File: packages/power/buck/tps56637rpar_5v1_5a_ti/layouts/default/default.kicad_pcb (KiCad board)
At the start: 2 copper layers, 10 parts

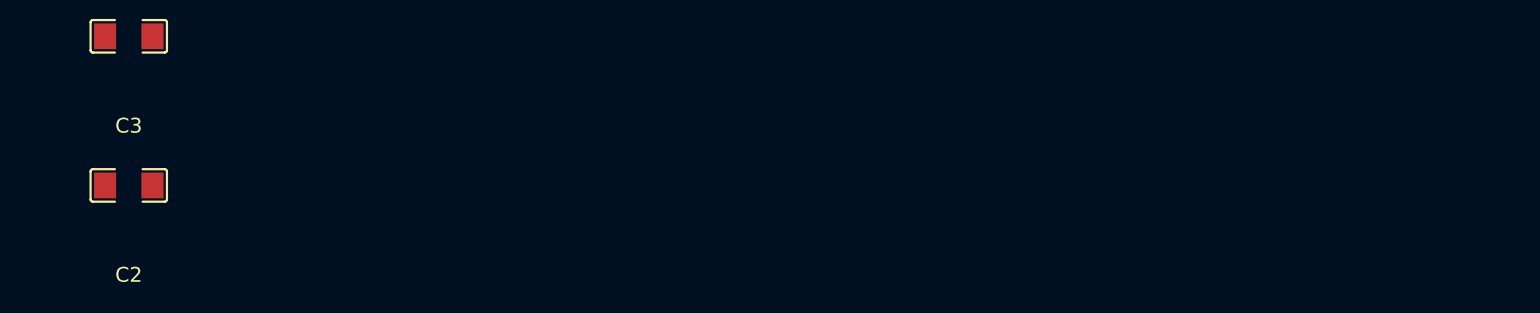
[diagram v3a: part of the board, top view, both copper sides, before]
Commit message: Keep package outputs aligned with production BOMs and documented parts
This removes top-level package example targets and their checked-in example
layouts so the library tracks the maintained default package outputs only.
It also adds minimal KiCad project files for each default layout and a
root components inventory derived from the top-level default BOMs, then
links that inventory from the repository guidance and README so future
part changes have one canonical summary.

Constraint: Package inventories must reflect explicit LCSC-traceable default BOM selections
Constraint: Default layouts need a KiCad project file in each package layout directory
Rejected: Keep example builds and layouts alongside default outputs | duplicated maintenance burden with little library value
Rejected: Build the component inventory from vendored part folders | would include non-fitted or non-purchasable items instead of actual package BOM contents
Confidence: high
Scope-risk: moderate
Reversibility: clean
Directive: When top-level package BOM contents change, update components_list.md in the same change
Tested:  in all 13 top-level packages
Tested:  for each added
Tested: Python validation that components_list.md LCSC codes exactly match all top-level default BOM JSON files
Not-tested: Interactive KiCad GUI opening of every project file
Not-tested: Any regenerated example targets or example layout workflows
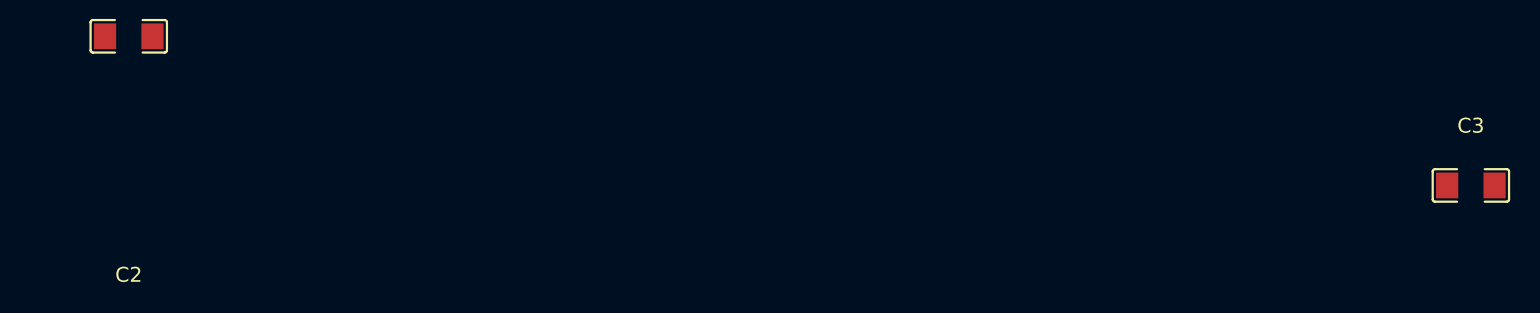
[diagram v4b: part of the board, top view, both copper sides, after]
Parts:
- moved C3 90.0 mm to (100.0, -50.0)
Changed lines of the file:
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@@
 	(footprint "Murata_Electronics_GRM31CR61H106KA12L:C1206"
 		(layer "F.Cu")
-		(at 10 -50 0)
+		(at 100 -50 0)
 		(property "Reference" "C3"
 			(at 0 -4)

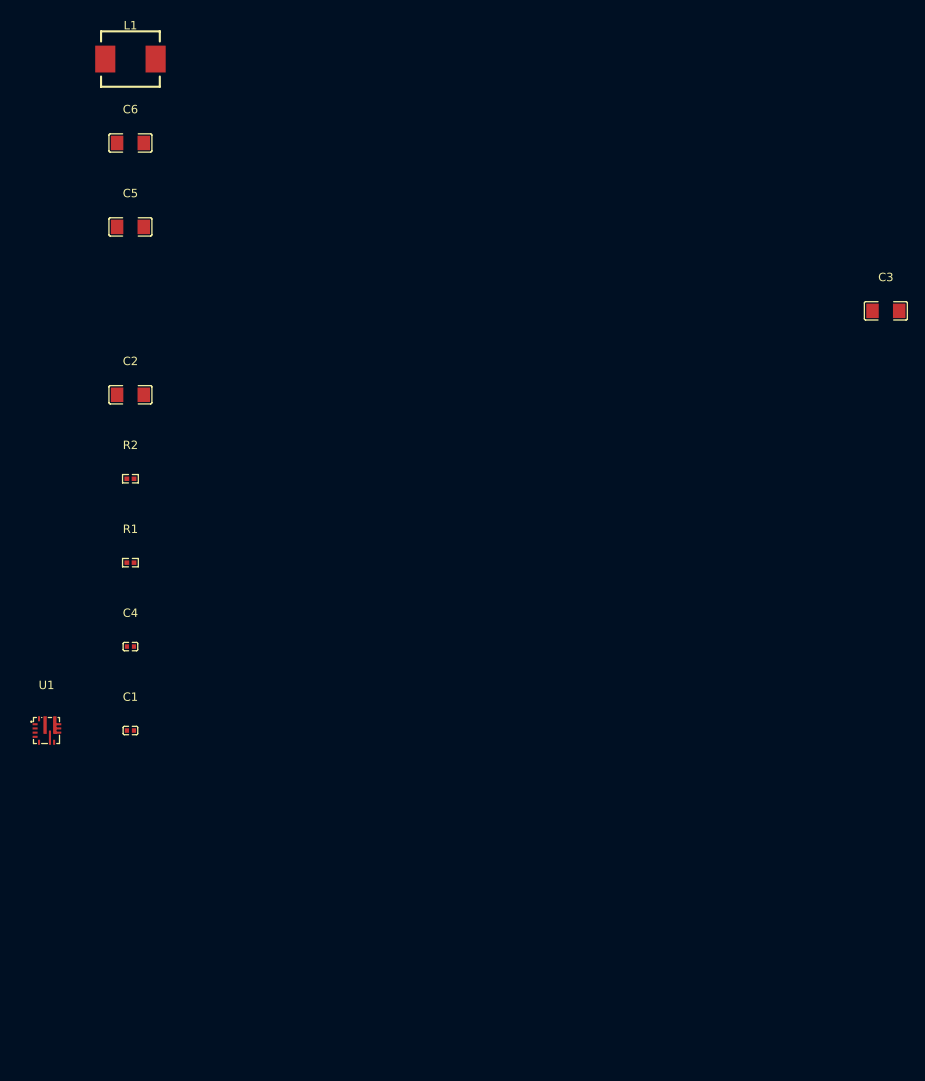
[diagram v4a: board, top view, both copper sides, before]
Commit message: 22uF cap update, TPS56637 update
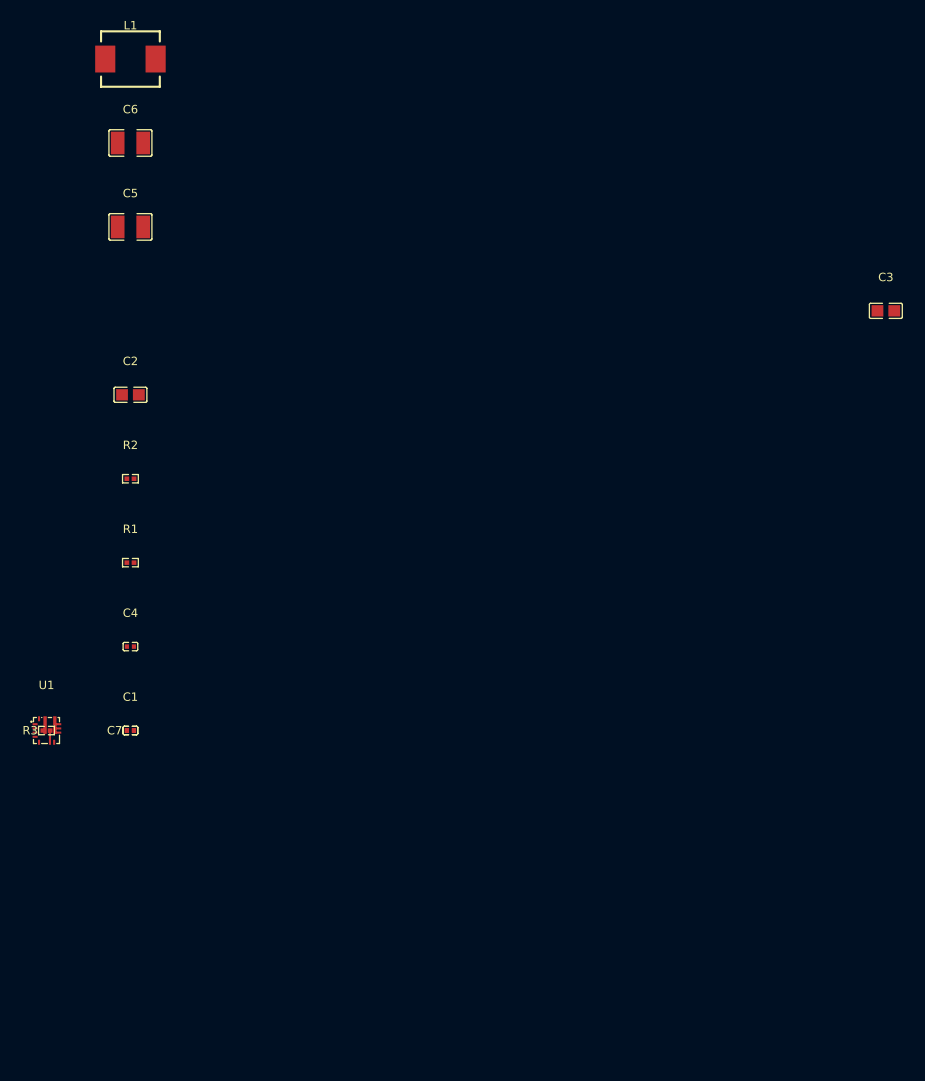
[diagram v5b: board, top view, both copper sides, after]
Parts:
- added C7: , Murata_Electronics_GRM1555C1H101JA01D:C0402, F.Cu at (10.0, 0.00)
- added R3: , YAGEO_RC0402FR_0720KL:R0402, F.Cu at (0.00, 0.00)
- C2, C3: footprint Murata_Electronics_GRM31CR61H106KA12L:C1206 -> Murata_Electronics_GRM21BR61H106KE43L:C0805
- C5, C6: footprint Murata_Electronics_GRM31CR61E226KE15L:C1206 -> Murata_Electronics_GRM32ER71E226KE15L:C1210

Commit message: TPS56637 layout
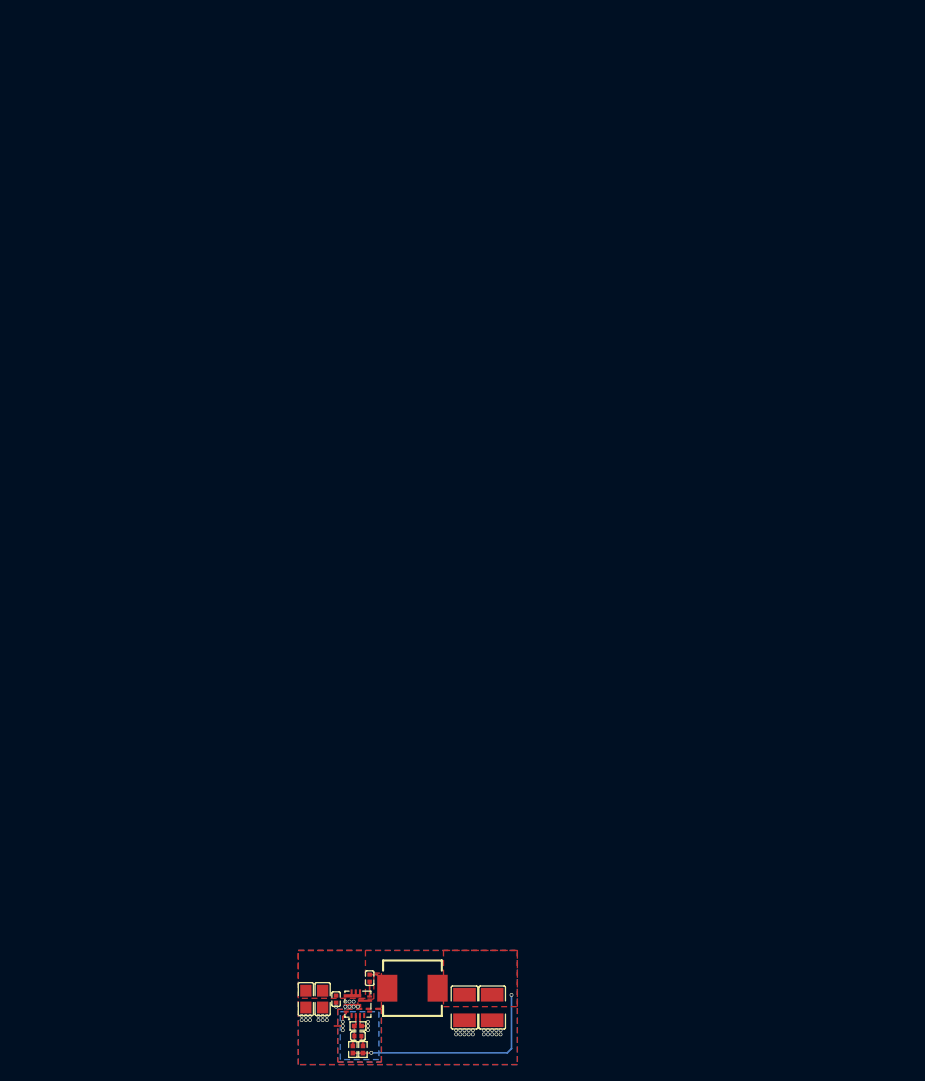
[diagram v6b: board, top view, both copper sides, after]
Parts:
- moved L1 115.7 mm to (43.6, 30.7)
- moved C6 110.4 mm to (49.8, 33.0), turned to -90 degrees
- moved C3 107.2 mm to (30.9, 32.0), turned to -90 degrees
- moved C5 102.5 mm to (53.1, 33.0), turned to -90 degrees
- moved C2 75.6 mm to (32.9, 32.0), turned to -90 degrees
- moved R2 73.0 mm to (36.5, 38.0), turned to 90 degrees
- moved R1 61.5 mm to (37.1, 35.2)
- moved R3 53.5 mm to (37.7, 38.0), turned to 90 degrees
- moved U1 49.4 mm to (37.1, 32.6), turned to 90 degrees
- moved C4 48.6 mm to (34.5, 32.0), turned to -90 degrees
- moved C7 45.4 mm to (37.1, 36.4), turned to 180 degrees
- moved C1 41.0 mm to (38.5, 29.5), turned to 90 degrees
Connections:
- U1 pad 10: MODE -> lv
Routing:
- net power_out-hv: track 0.00 -> 25.5 mm, vias 0 -> 2
- net lv: track 0.00 -> 6.46 mm, vias 0 -> 46
- net 2: track 0.00 -> 3.86 mm
- net SW: track 0.00 -> 3.01 mm
- net BOOT: track 0.00 -> 1.77 mm
- net 1: track 0.00 -> 1.34 mm
- added copper zone on F.Cu, net SW
- added copper zone on F.Cu, net hv
- added copper zone on B.Cu, net lv
- added copper zone on F.Cu, net lv
- added copper zone on In1.Cu, net lv
- added copper zone on In2.Cu, net lv
- added copper zone on F.Cu, net power_out-hv
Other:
- copper layers 2 -> 4

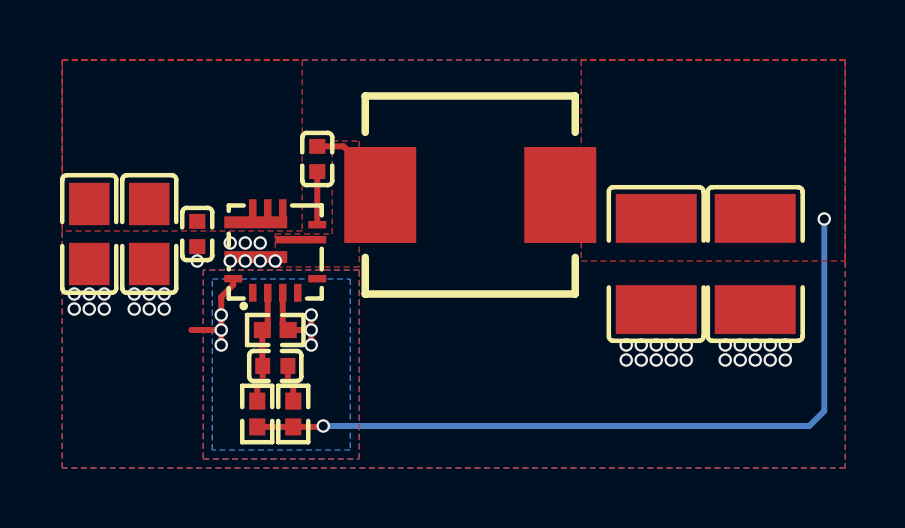
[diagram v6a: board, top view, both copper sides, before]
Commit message: TPS56637 update
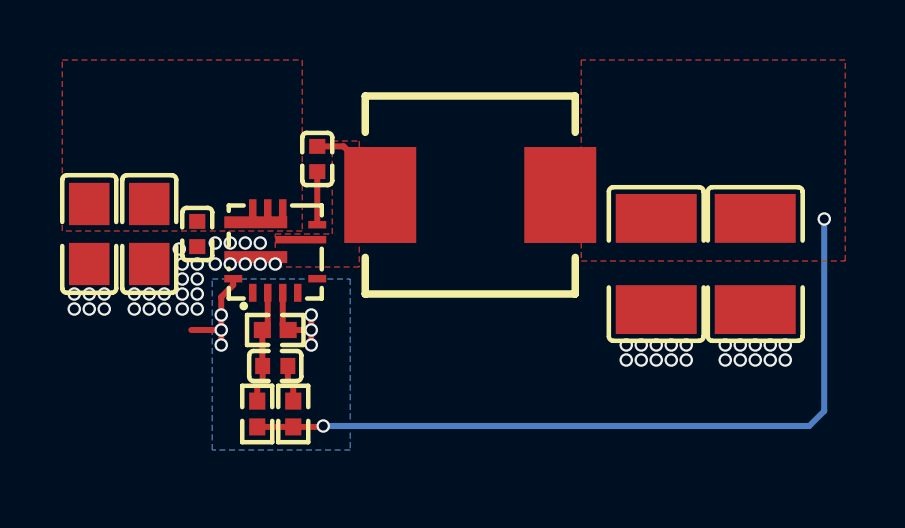
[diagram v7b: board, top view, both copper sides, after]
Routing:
- net lv: vias 46 -> 56
- removed copper zone on F.Cu, net lv
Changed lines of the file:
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@@
+	)
+	(via
+		(at 34 33.5)
+		(size 0.45)
+		(drill 0.3)
+		(layers "F.Cu" "B.Cu")
+		(free yes)
+		(net 6)
 	)
 	(via
@@
 	)
 	(via
+		(at 35.1 33)
+		(size 0.45)
+		(drill 0.3)
+		(layers "F.Cu" "B.Cu")
+		(free yes)
+		(net 6)
+	)
+	(via
 		(at 31.4 34.5)
 		(size 0.45)
@@
 	)
 	(via
+		(at 33.9 32.5)
+		(size 0.45)
+		(drill 0.3)
+		(layers "F.Cu" "B.Cu")
+		(free yes)
+		(net 6)
+	)
+	(via
 		(at 50.8 35.7)
 		(size 0.45)
@@
 	)
 	(via
-		(at 35.6 32.9)
+		(at 35.6 33)
 		(size 0.45)
 		(drill 0.3)
@@
 	)
 	(via
-		(at 37.1 32.9)
+		(at 37.1 33)
 		(size 0.45)
 		(drill 0.3)
@@
 	)
 	(via
+		(at 34 34.5)
+		(size 0.45)
+		(drill 0.3)
+		(layers "F.Cu" "B.Cu")
+		(free yes)
+		(net 6)
+	)
+	(via
 		(at 33.4 34.5)
 		(size 0.45)
@@
 	)
 	(via
+		(at 34.5 33)
+		(size 0.45)
+		(drill 0.3)
+		(layers "F.Cu" "B.Cu")
+		(free yes)
+		(net 6)
+	)
+	(via
 		(at 53.1 36.2)
 		(size 0.45)
@@
 	)
 	(via
-		(at 36.1 32.9)
+		(at 36.1 33)
 		(size 0.45)
 		(drill 0.3)
@@
 	)
 	(via
-		(at 34.5 32.9)
+		(at 34 33)
 		(size 0.45)
 		(drill 0.3)
@@
 	)
 	(via
+		(at 34.5 34)
+		(size 0.45)
+		(drill 0.3)
+		(layers "F.Cu" "B.Cu")
+		(free yes)
+		(net 6)
+	)
+	(via
 		(at 54.1 36.2)
 		(size 0.45)
@@
 	)
 	(via
+		(at 34 34)
+		(size 0.45)
+		(drill 0.3)
+		(layers "F.Cu" "B.Cu")
+		(free yes)
+		(net 6)
+	)
+	(via
 		(at 30.4 34)
 		(size 0.45)
@@
 	)
 	(via
+		(at 35.1 32.3)
+		(size 0.45)
+		(drill 0.3)
+		(layers "F.Cu" "B.Cu")
+		(free yes)
+		(net 6)
+	)
+	(via
 		(at 50.8 36.2)
 		(size 0.45)
@@
 	)
 	(via
-		(at 36.6 32.9)
+		(at 34.5 33.5)
+		(size 0.45)
+		(drill 0.3)
+		(layers "F.Cu" "B.Cu")
+		(free yes)
+		(net 6)
+	)
+	(via
+		(at 34.5 34.5)
+		(size 0.45)
+		(drill 0.3)
+		(layers "F.Cu" "B.Cu")
+		(free yes)
+		(net 6)
+	)
+	(via
+		(at 36.6 33)
 		(size 0.45)
 		(drill 0.3)
@@
 	)
 	(zone
+		(net 0)
+		(net_name "")
+		(layer "F.Cu")
+		(hatch edge 0.5)
+		(connect_pads yes
+			(clearance 0)
+		)
+		(min_thickness 0.25)
+		(filled_areas_thickness no)
+		(keepout
+			(tracks allowed)
+			(vias allowed)
+			(pads allowed)
+			(copperpour not_allowed)
+			(footprints allowed)
+		)
+		(placement
+			(enabled no)
+			(sheetname "")
+		)
+		(fill
+			(thermal_gap 0.5)
+			(thermal_bridge_width 0.5)
+		)
+		(polygon
+			(pts
+				(xy 35 33.5) (xy 39.6 33.5) (xy 39.6 39.2) (xy 35 39.2)
+			)
+		)
+	)
+	(zone
 		(net 5)
 		(net_name "hv")
@@
 	)
 	(zone
-		(net 6)
-		(net_name "lv")
+		(net 0)
+		(net_name "")
 		(layers "F.Cu" "B.Cu" "In1.Cu" "In2.Cu")
 		(hatch edge 0.5)
 		(connect_pads yes
-			(clearance 0.2)
+			(clearance 0)
 		)
 		(min_thickness 0.25)
 		(filled_areas_thickness no)
-		(fill yes
+		(keepout
+			(tracks allowed)
+			(vias allowed)
+			(pads allowed)
+			(copperpour not_allowed)
+			(footprints allowed)
+		)
+		(placement
+			(enabled no)
+			(sheetname "")
+		)
+		(fill
 			(thermal_gap 0.5)
 			(thermal_bridge_width 0.5)
@@
 		(polygon
 			(pts
-				(xy 56.1 39.8) (xy 30 39.8) (xy 30 26.2) (xy 56.1 26.2)
+				(xy 39.8 39.4) (xy 34.8 39.4) (xy 34.8 33.3) (xy 39.8 33.3)
 			)
 		)
 		(polygon
 			(pts
-				(xy 34.7 33.2) (xy 34.7 39.5) (xy 39.9 39.5) (xy 39.9 33.2)
+				(xy 35 33.5) (xy 35 39.2) (xy 39.6 39.2) (xy 39.6 33.5)
 			)
 		)
